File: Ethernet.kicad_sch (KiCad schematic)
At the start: 6 parts, among them J401 J1V-U2100NL, U401 TPD4EUSB30, U402 TPD4EUSB30

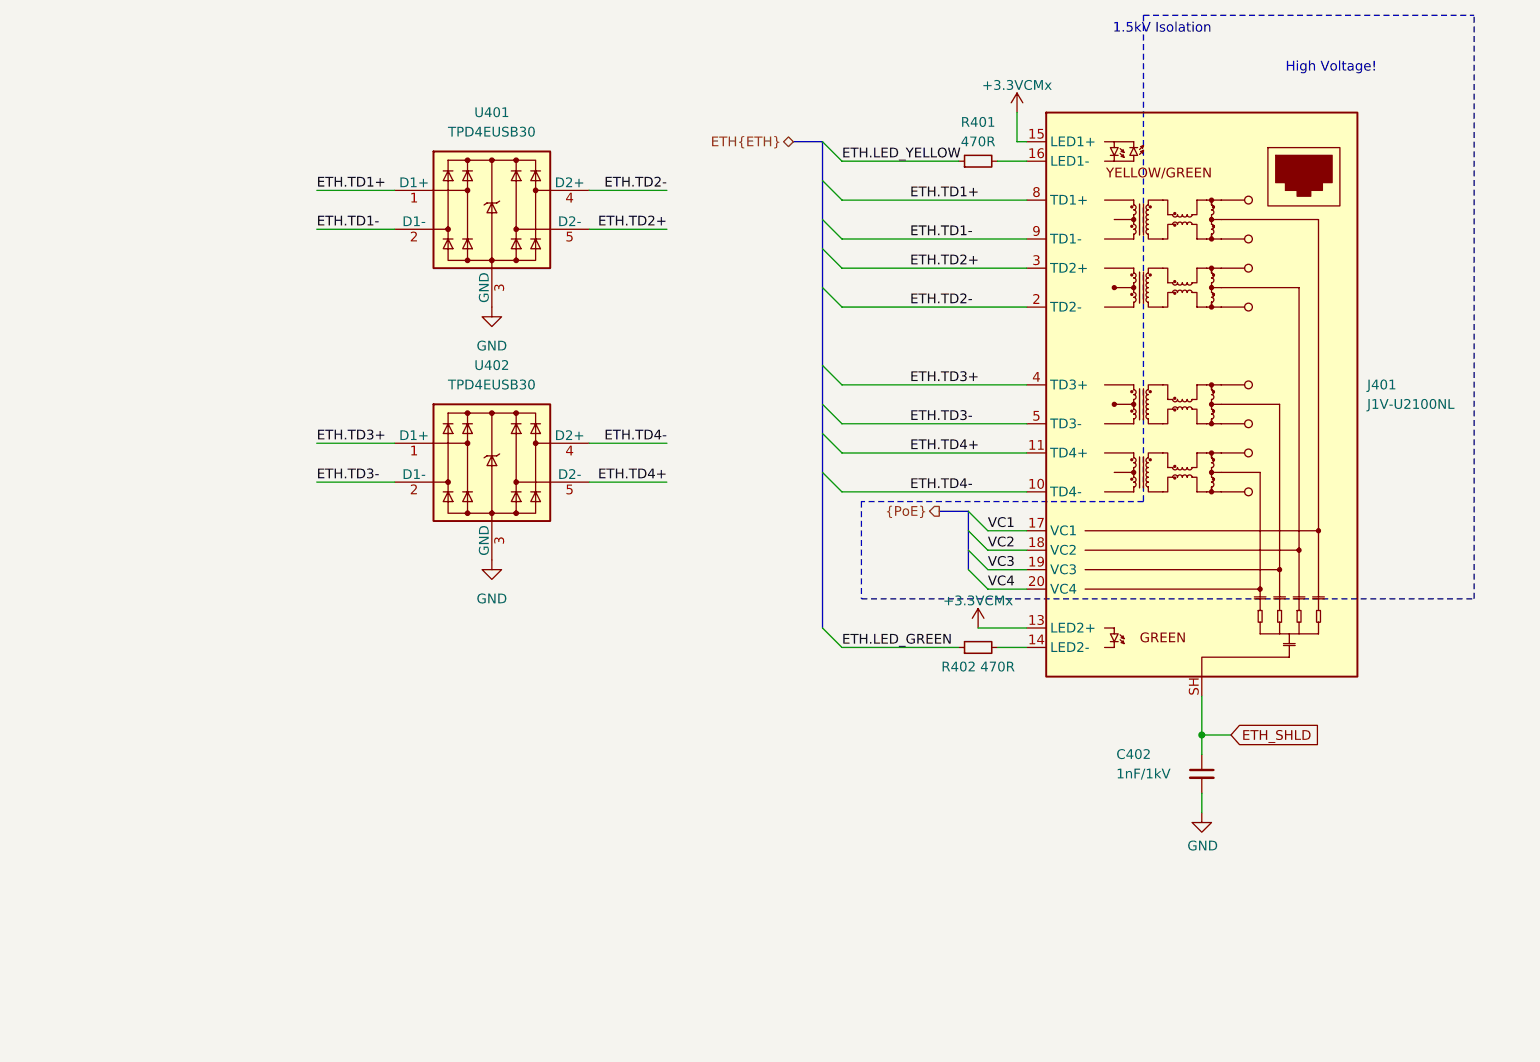
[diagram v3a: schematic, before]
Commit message: Partial trace layout, kick-ass custom rules
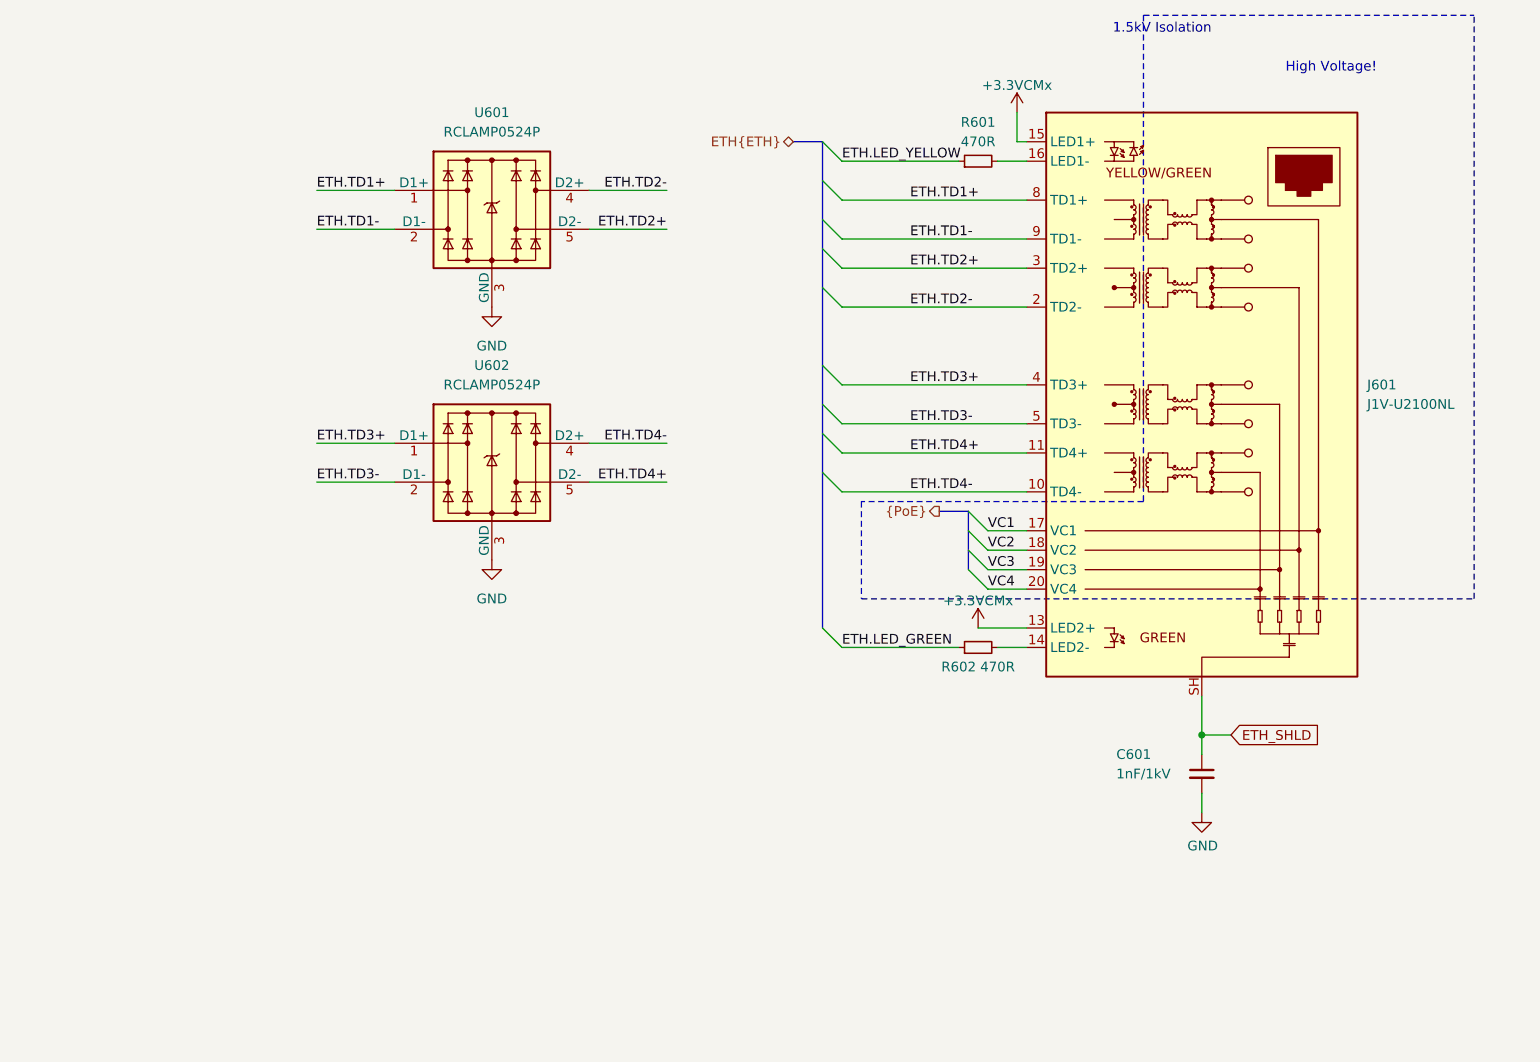
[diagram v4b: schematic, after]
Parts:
- U601: renamed from U401; value TPD4EUSB30 -> RCLAMP0524P; LCSC C558427 -> C907837
- U602: renamed from U402; value TPD4EUSB30 -> RCLAMP0524P; LCSC C558427 -> C907837
- renumbered C402 to C601, J401 to J601, R401 to R601, R402 to R602
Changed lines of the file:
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@@
 	(label "ETH.TD1+"
 		(at 139.7 60.96 0)
-		(fields_autoplaced yes)
 		(effects
 			(font
@@
 	(label "VC2"
 		(at 149.86 106.68 0)
-		(fields_autoplaced yes)
 		(effects
 			(font
@@
 	(label "ETH.TD2-"
 		(at 107.95 59.69 180)
-		(fields_autoplaced yes)
 		(effects
 			(font
@@
 	(label "ETH.TD4-"
 		(at 107.95 92.71 180)
-		(fields_autoplaced yes)
 		(effects
 			(font
@@
 	(label "ETH.TD1-"
 		(at 139.7 66.04 0)
-		(fields_autoplaced yes)
 		(effects
 			(font
@@
 	(label "ETH.TD3+"
 		(at 62.23 92.71 0)
-		(fields_autoplaced yes)
 		(effects
 			(font
@@
 	(label "ETH.TD2+"
 		(at 107.95 64.77 180)
-		(fields_autoplaced yes)
 		(effects
 			(font
@@
 	(label "ETH.TD2-"
 		(at 139.7 74.93 0)
-		(fields_autoplaced yes)
 		(effects
 			(font
@@
 	(label "ETH.TD1+"
 		(at 62.23 59.69 0)
-		(fields_autoplaced yes)
 		(effects
 			(font
@@
 	(label "ETH.TD4+"
 		(at 107.95 97.79 180)
-		(fields_autoplaced yes)
 		(effects
 			(font
@@
 	(label "ETH.TD3+"
 		(at 139.7 85.09 0)
-		(fields_autoplaced yes)
 		(effects
 			(font
@@
 	(label "VC3"
 		(at 149.86 109.22 0)
-		(fields_autoplaced yes)
 		(effects
 			(font
@@
 	(label "ETH.TD3-"
 		(at 62.23 97.79 0)
-		(fields_autoplaced yes)
 		(effects
 			(font
@@
 	(label "ETH.LED_GREEN"
 		(at 130.81 119.38 0)
-		(fields_autoplaced yes)
 		(effects
 			(font
@@
 	(label "ETH.TD1-"
 		(at 62.23 64.77 0)
-		(fields_autoplaced yes)
 		(effects
 			(font
@@
 	(label "ETH.TD2+"
 		(at 139.7 69.85 0)
-		(fields_autoplaced yes)
 		(effects
 			(font
@@
 	(label "VC4"
 		(at 149.86 111.76 0)
-		(fields_autoplaced yes)
 		(effects
 			(font
@@
 	(label "ETH.TD4+"
 		(at 139.7 93.98 0)
-		(fields_autoplaced yes)
 		(effects
 			(font
@@
 	(label "ETH.LED_YELLOW"
 		(at 130.81 55.88 0)
-		(fields_autoplaced yes)
 		(effects
 			(font
@@
 	(label "ETH.TD3-"
 		(at 139.7 90.17 0)
-		(fields_autoplaced yes)
 		(effects
 			(font
@@
 	(label "ETH.TD4-"
 		(at 139.7 99.06 0)
-		(fields_autoplaced yes)
 		(effects
 			(font
@@
 	(label "VC1"
 		(at 149.86 104.14 0)
-		(fields_autoplaced yes)
 		(effects
 			(font
@@
 		(shape output)
 		(at 143.51 101.6 180)
-		(fields_autoplaced yes)
 		(effects
 			(font
@@
 		(shape bidirectional)
 		(at 124.46 53.34 180)
-		(fields_autoplaced yes)
 		(effects
 			(font
@@
 		(on_board yes)
 		(dnp no)
-		(property "Reference" "#PWR0404"
+		(property "Reference" "#PWR0604"
 			(at 148.59 120.65 0)
 			(effects
@@
 			(project "Yellow"
 				(path "/abc482bd-3f17-4d35-80db-1da3dcdb5c27/18c18357-12fa-4472-a108-e954e5bd7840"
-					(reference "#PWR0404")
+					(reference "#PWR0604")
 					(unit 1)
 				)
@@
 		(on_board yes)
 		(dnp no)
-		(property "Reference" "R402"
+		(property "Reference" "R602"
 			(at 146.05 121.92 90)
 			(effects
@@
 		)
 		(property "LCSC" "C25117"
-			(at 148.59 119.38 0)
-			(effects
-				(font
-					(size 1.27 1.27)
-				)
-				(hide yes)
-			)
-		)
-		(property "Sim.Enable" ""
 			(at 148.59 119.38 0)
 			(effects
@@
 			(project "Yellow"
 				(path "/abc482bd-3f17-4d35-80db-1da3dcdb5c27/18c18357-12fa-4472-a108-e954e5bd7840"
-					(reference "R402")
+					(reference "R602")
 					(unit 1)
 				)
@@
 		(on_board yes)
 		(dnp no)
-		(property "Reference" "C402"
+		(property "Reference" "C601"
 			(at 168.91 133.35 0)
 			(effects
@@
 		)
 		(property "LCSC" "C1941"
-			(at 177.8 135.89 0)
-			(effects
-				(font
-					(size 1.27 1.27)
-				)
-				(hide yes)
-			)
-		)
-		(property "Sim.Enable" ""
 			(at 177.8 135.89 0)
 			(effects
@@
 			(project "Yellow"
 				(path "/abc482bd-3f17-4d35-80db-1da3dcdb5c27/18c18357-12fa-4472-a108-e954e5bd7840"
-					(reference "C402")
+					(reference "C601")
 					(unit 1)
 				)
@@
 		(dnp no)
 		(fields_autoplaced yes)
-		(property "Reference" "#PWR0401"
+		(property "Reference" "#PWR0602"
 			(at 85.09 81.28 0)
 			(effects
@@
 			(project "Yellow"
 				(path "/abc482bd-3f17-4d35-80db-1da3dcdb5c27/18c18357-12fa-4472-a108-e954e5bd7840"
-					(reference "#PWR0401")
+					(reference "#PWR0602")
 					(unit 1)
 				)
@@
 		(on_board yes)
 		(dnp no)
-		(property "Reference" "U402"
+		(property "Reference" "U602"
 			(at 85.09 82.55 0)
 			(effects
@@
 			)
 		)
-		(property "Value" "TPD4EUSB30"
+		(property "Value" "RCLAMP0524P"
 			(at 85.09 85.09 0)
 			(effects
@@
 			)
 		)
-		(property "LCSC" "C558427"
-			(at 85.09 95.25 0)
-			(effects
-				(font
-					(size 1.27 1.27)
-				)
-				(hide yes)
-			)
-		)
-		(property "Sim.Enable" ""
+		(property "LCSC" "C907837"
 			(at 85.09 95.25 0)
 			(effects
@@
 			(project "Yellow"
 				(path "/abc482bd-3f17-4d35-80db-1da3dcdb5c27/18c18357-12fa-4472-a108-e954e5bd7840"
-					(reference "U402")
+					(reference "U602")
 					(unit 1)
 				)
@@
 		(on_board yes)
 		(dnp no)
-		(property "Reference" "R401"
+		(property "Reference" "R601"
 			(at 148.59 50.8 90)
 			(effects
@@
 		)
 		(property "LCSC" "C25117"
-			(at 148.59 55.88 0)
-			(effects
-				(font
-					(size 1.27 1.27)
-				)
-				(hide yes)
-			)
-		)
-		(property "Sim.Enable" ""
 			(at 148.59 55.88 0)
 			(effects
@@
 			(project "Yellow"
 				(path "/abc482bd-3f17-4d35-80db-1da3dcdb5c27/18c18357-12fa-4472-a108-e954e5bd7840"
-					(reference "R401")
+					(reference "R601")
 					(unit 1)
 				)
@@
 		(dnp no)
 		(fields_autoplaced yes)
-		(property "Reference" "J401"
+		(property "Reference" "J601"
 			(at 199.39 85.0899 0)
 			(effects
@@
 		)
 		(property "LCSC" "C3179838"
-			(at 177.8 86.36 0)
-			(effects
-				(font
-					(size 1.27 1.27)
-				)
-				(hide yes)
-			)
-		)
-		(property "Sim.Enable" ""
 			(at 177.8 86.36 0)
 			(effects
@@
 			(project "Yellow"
 				(path "/abc482bd-3f17-4d35-80db-1da3dcdb5c27/18c18357-12fa-4472-a108-e954e5bd7840"
-					(reference "J401")
+					(reference "J601")
 					(unit 1)
 				)
@@
 		(on_board yes)
 		(dnp no)
-		(property "Reference" "#PWR0406"
+		(property "Reference" "#PWR0605"
 			(at 177.8 147.32 0)
 			(effects
@@
 			(project "Yellow"
 				(path "/abc482bd-3f17-4d35-80db-1da3dcdb5c27/18c18357-12fa-4472-a108-e954e5bd7840"
-					(reference "#PWR0406")
+					(reference "#PWR0605")
 					(unit 1)
 				)
@@
 		(dnp no)
 		(fields_autoplaced yes)
-		(property "Reference" "#PWR0402"
+		(property "Reference" "#PWR0603"
 			(at 85.09 114.3 0)
 			(effects
@@
 			(project "Yellow"
 				(path "/abc482bd-3f17-4d35-80db-1da3dcdb5c27/18c18357-12fa-4472-a108-e954e5bd7840"
-					(reference "#PWR0402")
+					(reference "#PWR0603")
 					(unit 1)
 				)
@@
 		(on_board yes)
 		(dnp no)
-		(property "Reference" "U401"
+		(property "Reference" "U601"
 			(at 85.09 49.53 0)
 			(effects
@@
 			)
 		)
-		(property "Value" "TPD4EUSB30"
+		(property "Value" "RCLAMP0524P"
 			(at 85.09 52.07 0)
 			(effects
@@
 			)
 		)
-		(property "LCSC" "C558427"
-			(at 85.09 62.23 0)
-			(effects
-				(font
-					(size 1.27 1.27)
-				)
-				(hide yes)
-			)
-		)
-		(property "Sim.Enable" ""
+		(property "LCSC" "C907837"
 			(at 85.09 62.23 0)
 			(effects
@@
 			(project "Yellow"
 				(path "/abc482bd-3f17-4d35-80db-1da3dcdb5c27/18c18357-12fa-4472-a108-e954e5bd7840"
-					(reference "U401")
+					(reference "U601")
 					(unit 1)
 				)
@@
 		(on_board yes)
 		(dnp no)
-		(property "Reference" "#PWR0405"
+		(property "Reference" "#PWR0601"
 			(at 153.67 53.34 0)
 			(effects
@@
 			(project "Yellow"
 				(path "/abc482bd-3f17-4d35-80db-1da3dcdb5c27/18c18357-12fa-4472-a108-e954e5bd7840"
-					(reference "#PWR0405")
+					(reference "#PWR0601")
 					(unit 1)
 				)

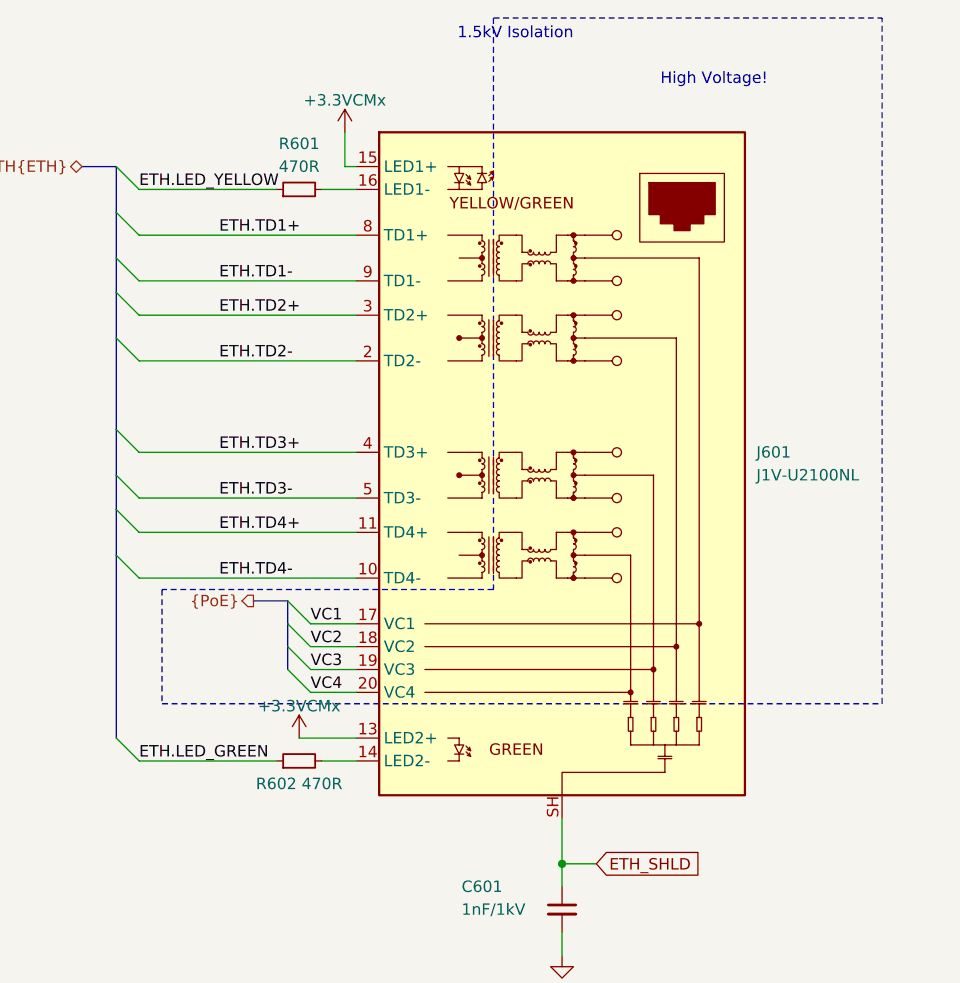
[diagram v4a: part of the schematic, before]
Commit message: Remove PoE support
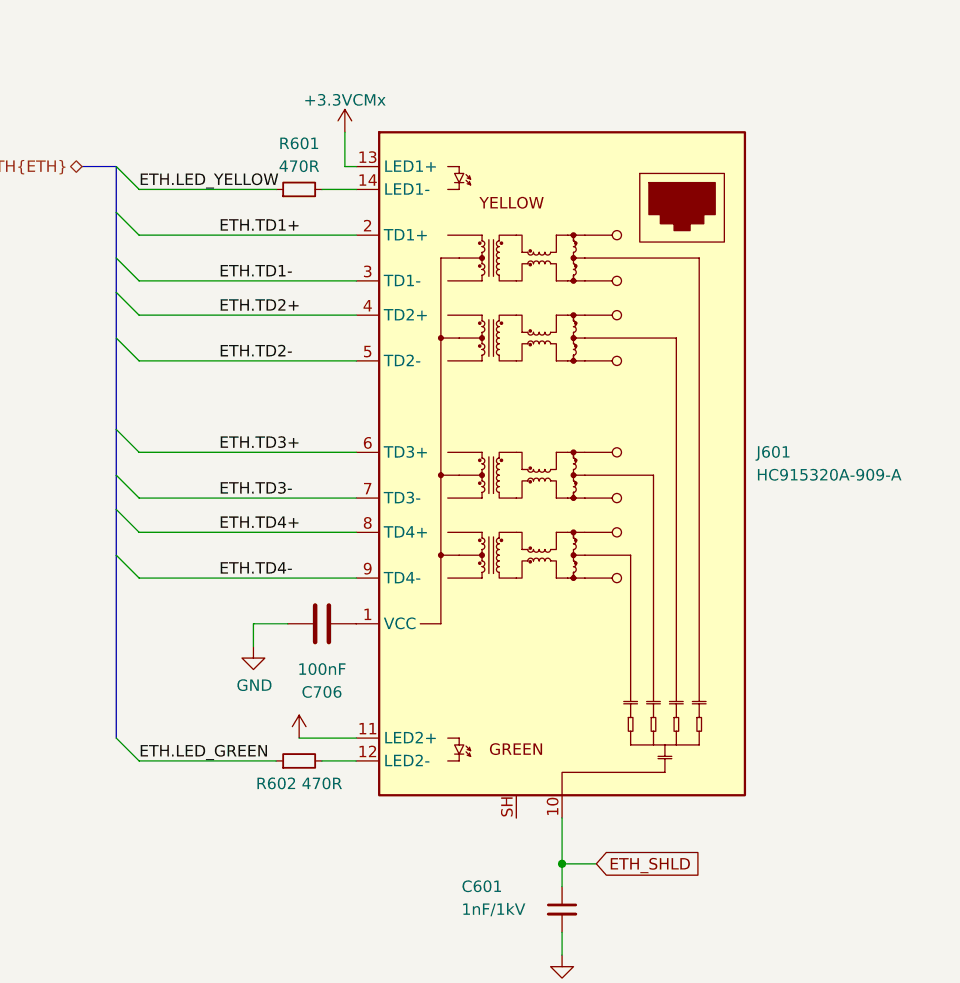
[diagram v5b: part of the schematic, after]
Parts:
- added C706: 100nF, Capacitor_SMD:C_0402_1005Metric, symbol Device:C
- J601: value J1V-U2100NL -> HC915320A-909-A; footprint Hatlabs:RJ45_Pulse_J1V_U2100NL_Vertical -> Hatlabs:RJ45_HC915320A-909-A_Vertical; symbol Hatlabs:RJ45_Pulse_J1V-U2100NL_Vertical -> Hatlabs:RJ45_HCTL_HC915320A-909-A_Vertical; LCSC C3179838 -> C5341220
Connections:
- net +3.3VCMx: now also J601.11 (LED2+); no longer J601.15 (LED1+)
- net ETH.TD1+: now also J601.2 (TD1+); no longer J601.8 (TD1+)
- net ETH.TD1-: now also J601.3 (TD1-); no longer J601.9 (TD1-)
- net ETH.TD2+: now also J601.4 (TD2+); no longer J601.3 (TD2+)
- net ETH.TD2-: now also J601.5 (TD2-); no longer J601.2 (TD2-)
- net ETH.TD3+: now also J601.6 (TD3+); no longer J601.4 (TD3+)
- net ETH.TD3-: now also J601.7 (TD3-); no longer J601.5 (TD3-)
- net ETH.TD4+: now also J601.8 (TD4+); no longer J601.11 (TD4+)
- net ETH.TD4-: now also J601.9 (TD4-); no longer J601.10 (TD4-)
- net ETH_SHLD: now also J601.10; no longer J601.SH
- net GND: now also C706.2
- net at R602.2: now also J601.12 (LED2-); no longer J601.14 (LED2-)
- net at R601.2: now also J601.14 (LED1-); no longer J601.16 (LED1-)
- net at J601.1 (VCC): now also C706.1
- removed net VC1: J601.17 (VC1)
- removed net VC2: J601.18 (VC2)
- removed net VC3: J601.19 (VC3)
- removed net VC4: J601.20 (VC4)
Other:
- note removed: "1.5kV Isolation"
- note removed: "High Voltage!"

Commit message: Move to a two-sided assembly
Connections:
- net ETH.TD2+: now also U601.4 (D2+), U601.7 (D2+); no longer U601.5 (D2-), U601.6 (D2-)
- net ETH.TD2-: now also U601.5 (D2-), U601.6 (D2-); no longer U601.4 (D2+), U601.7 (D2+)
- net ETH.TD4+: now also U602.4 (D2+), U602.7 (D2+); no longer U602.5 (D2-), U602.6 (D2-)
- net ETH.TD4-: now also U602.5 (D2-), U602.6 (D2-); no longer U602.4 (D2+), U602.7 (D2+)
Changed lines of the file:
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@@
 	)
 	(label "ETH.TD2-"
-		(at 107.95 59.69 180)
+		(at 107.95 64.77 180)
 		(effects
 			(font
@@
 	)
 	(label "ETH.TD4-"
-		(at 107.95 92.71 180)
+		(at 107.95 97.79 180)
 		(effects
 			(font
@@
 	)
 	(label "ETH.TD2+"
-		(at 107.95 64.77 180)
+		(at 107.95 59.69 180)
 		(effects
 			(font
@@
 	)
 	(label "ETH.TD4+"
-		(at 107.95 97.79 180)
+		(at 107.95 92.71 180)
 		(effects
 			(font
